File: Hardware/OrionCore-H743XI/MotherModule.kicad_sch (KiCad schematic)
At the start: 1 part, among them U2 STM32H743XIHx

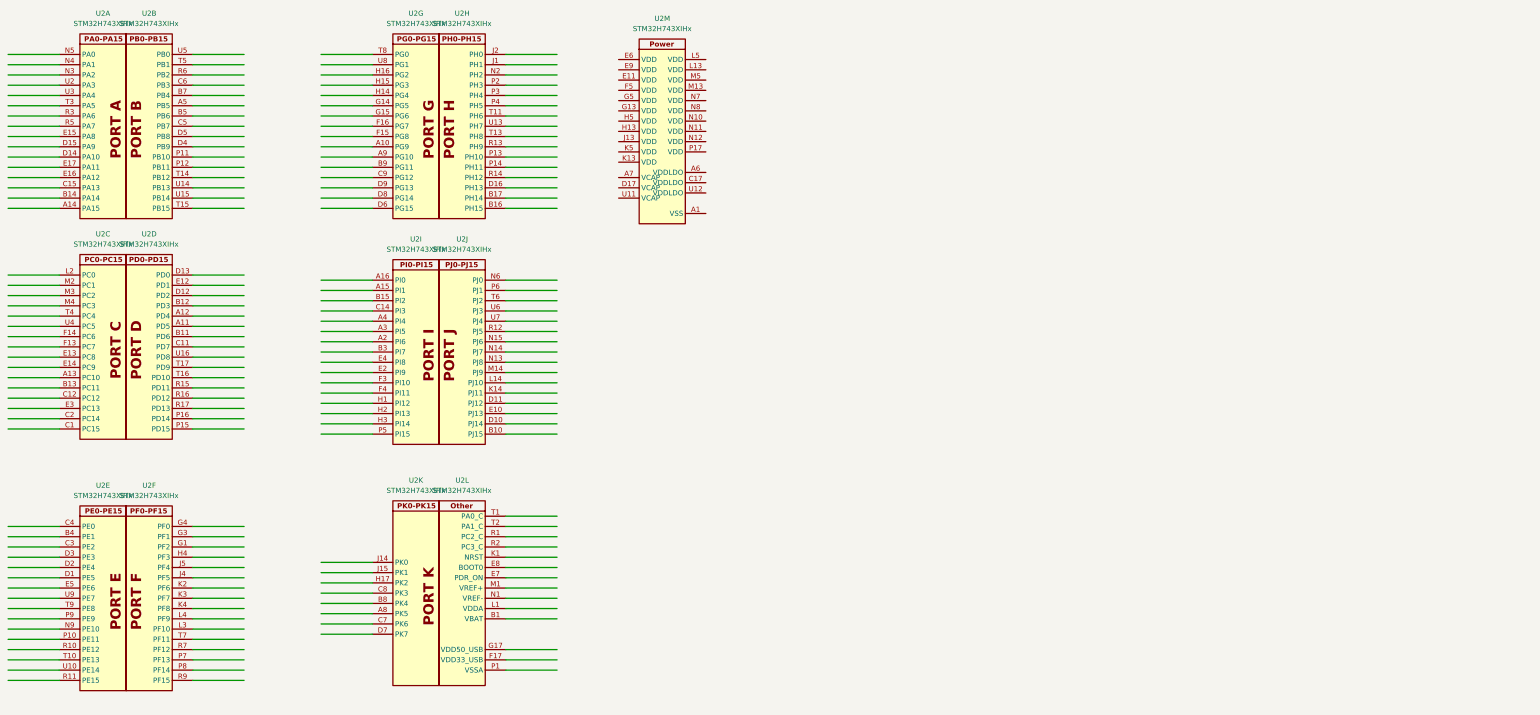
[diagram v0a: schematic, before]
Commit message: Update SDRAM, RGB LCD, QSPI Flash Pin
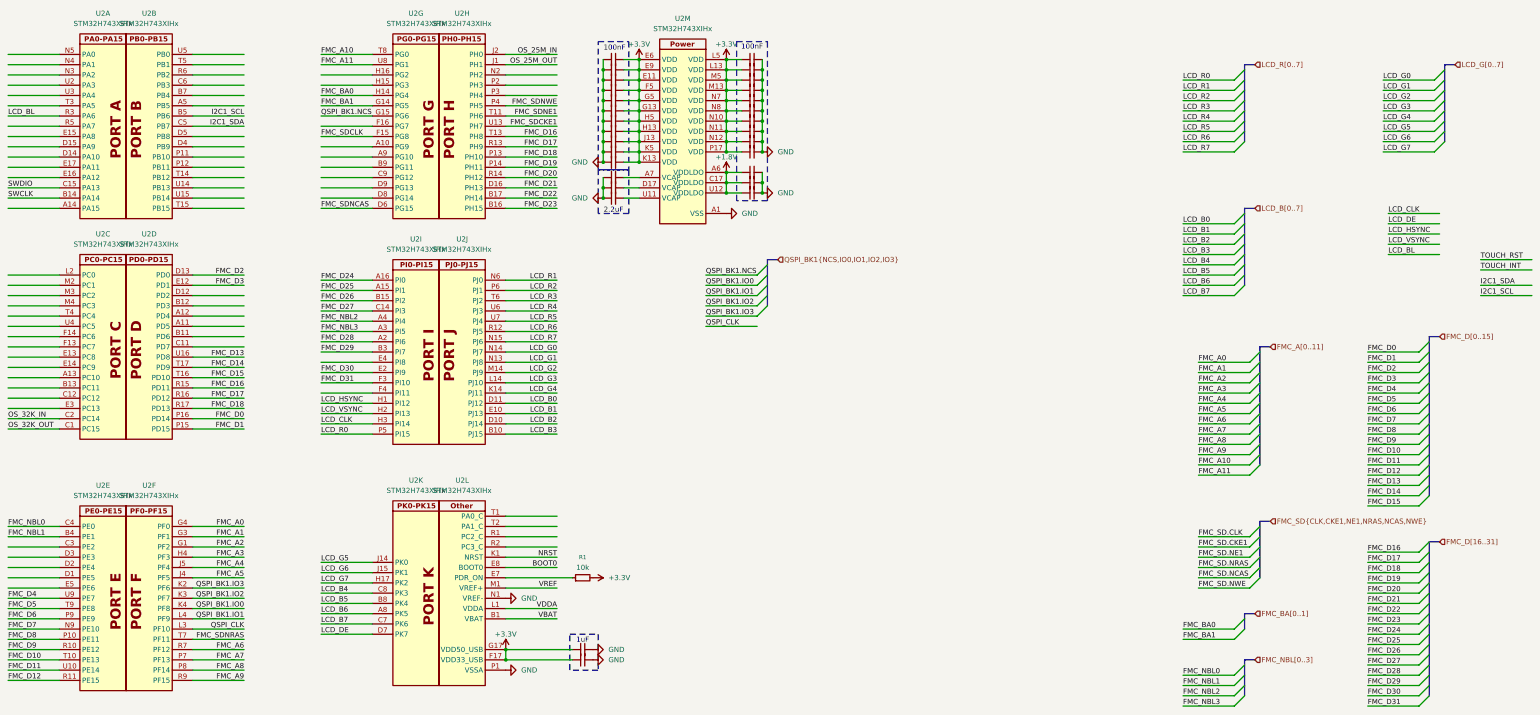
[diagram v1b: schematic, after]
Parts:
- added C1, C2: 1uF, Capacitor_SMD:C_0201_0603Metric, symbol Device:C_Small
- added C10, C11, C12, C13, C14, C15, C16, C17, C18, C19, C20, C21, C22, C23, C24, C25, C26, C3, C4, C5, C6, C7, C8, C9: 100nF, Capacitor_SMD:C_0201_0603Metric, symbol Device:C_Small
- added C27, C28, C29: 2.2uF, Capacitor_SMD:C_0402_1005Metric, symbol Device:C_Small
- added R1: 10k, Resistor_SMD:R_0201_0603Metric, symbol Device:R_Small
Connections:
- net VBAT: now reaches U2.B1 (VBAT)
- net at U2.E7 (PDR_ON): now also R1.1
- net BOOT0: now reaches U2.E8 (BOOT0)
- net +3.3V: now reaches U2.F17 (VDD33_USB)
- net +3.3V: now also U2.E11 (VDD), U2.E6 (VDD), U2.E9 (VDD), U2.F5 (VDD), U2.G13 (VDD), U2.G17 (VDD50_USB), U2.G5 (VDD), U2.H13 (VDD), U2.H5 (VDD), U2.J13 (VDD), U2.K13 (VDD), U2.K5 (VDD), U2.L13 (VDD), U2.L5 (VDD), U2.M13 (VDD), U2.M5 (VDD), U2.N10 (VDD), U2.N11 (VDD), U2.N12 (VDD), U2.N7 (VDD), U2.N8 (VDD), U2.P17 (VDD), C1.1, C10.1, C11.1, C12.1, C13.1, C14.1, C15.1, C16.1, C17.1, C18.1, C19.1, C2.1, C20.1, C21.1, C22.1, C23.1, C24.1, C25.1, C26.1, C6.1, C7.1, C8.1, C9.1, R1.2
- net NRST: now reaches U2.K1 (NRST)
- net VDDA: now reaches U2.L1 (VDDA)
- net VREF: now reaches U2.M1 (VREF+)
- net GND: now reaches U2.N1 (VREF-)
- net GND: now also U2.A1 (VSS), U2.A17 (VSS), U2.B2 (VSS), U2.B6 (VSS), U2.C10 (VSS), U2.C13 (VSS), U2.C16 (VSS), U2.F1 (VSS), U2.F2 (VSS), U2.G10 (VSS), U2.G11 (VSS), U2.G16 (VSS), U2.G2 (VSS), U2.G7 (VSS), U2.G8 (VSS), U2.G9 (VSS), U2.H10 (VSS), U2.H11 (VSS), U2.H7 (VSS), U2.H8 (VSS), U2.H9 (VSS), U2.J10 (VSS), U2.J11 (VSS), U2.J16 (VSS), U2.J17 (VSS), U2.J3 (VSS), U2.J7 (VSS), U2.J8 (VSS), U2.J9 (VSS), U2.K10 (VSS), U2.K11 (VSS), U2.K15 (VSS), U2.K7 (VSS), U2.K8 (VSS), U2.K9 (VSS), U2.L10 (VSS), U2.L11 (VSS), U2.L15 (VSS), U2.L7 (VSS), U2.L8 (VSS), U2.L9 (VSS), U2.M15 (VSS), U2.N16 (VSS), U2.P1 (VSSA), U2.R4 (VSS), U2.R8 (VSS), U2.T12 (VSS), U2.U1 (VSS), U2.U17 (VSS), C1.2, C10.2, C11.2, C12.2, C13.2, C14.2, C15.2, C16.2, C17.2, C18.2, C19.2, C2.2, C20.2, C21.2, C22.2, C23.2, C24.2, C25.2, C26.2, C27.1, C28.1, C29.1, C3.2, C4.2, C5.2, C6.2, C7.2, C8.2, C9.2
- net FMC_D25: now reaches U2.A15 (PI1)
- net FMC_D24: now reaches U2.A16 (PI0)
- net FMC_D28: now reaches U2.A2 (PI6)
- net FMC_NBL3: now reaches U2.A3 (PI5)
- net FMC_NBL2: now reaches U2.A4 (PI4)
- net FMC_D26: now reaches U2.B15 (PI2)
- net FMC_D29: now reaches U2.B3 (PI7)
- net FMC_D27: now reaches U2.C14 (PI3)
- net FMC_D30: now reaches U2.E2 (PI9)
- net FMC_D31: now reaches U2.F3 (PI10)
- net LCD_HSYNC: now reaches U2.H1 (PI12)
- net LCD_VSYNC: now reaches U2.H2 (PI13)
- net LCD_CLK: now reaches U2.H3 (PI14)
- net LCD_R0: now reaches U2.P5 (PI15)
- net FMC_NBL1: now reaches U2.B4 (PE1)
- net FMC_NBL0: now reaches U2.C4 (PE0)
- net FMC_D7: now reaches U2.N9 (PE10)
- net FMC_D8: now reaches U2.P10 (PE11)
- net FMC_D6: now reaches U2.P9 (PE9)
- net FMC_D9: now reaches U2.R10 (PE12)
- net FMC_D12: now reaches U2.R11 (PE15)
- net FMC_D10: now reaches U2.T10 (PE13)
- net FMC_D5: now reaches U2.T9 (PE8)
- net FMC_D11: now reaches U2.U10 (PE14)
- net FMC_D4: now reaches U2.U9 (PE7)
- net SWCLK: now reaches U2.B14 (PA14)
- net SWDIO: now reaches U2.C15 (PA13)
- net LCD_BL: now reaches U2.R3 (PA6)
- net FMC_D2: now reaches U2.D13 (PD0)
- net FMC_D3: now reaches U2.E12 (PD1)
- net FMC_D1: now reaches U2.P15 (PD15)
- net FMC_D0: now reaches U2.P16 (PD14)
- net FMC_D16: now reaches U2.R15 (PD11)
- net FMC_D16: now also U2.T13 (PH8)
- net FMC_D17: now reaches U2.R16 (PD12)
- net FMC_D17: now also U2.R13 (PH9)
- net FMC_D18: now reaches U2.R17 (PD13)
- net FMC_D18: now also U2.P13 (PH10)
- net FMC_D15: now reaches U2.T16 (PD10)
- net FMC_D14: now reaches U2.T17 (PD9)
- net FMC_D13: now reaches U2.U16 (PD8)
- net LCD_B6: now reaches U2.A8 (PK5)
- net LCD_B5: now reaches U2.B8 (PK4)
- net LCD_B7: now reaches U2.C7 (PK6)
- net LCD_B4: now reaches U2.C8 (PK3)
- net LCD_DE: now reaches U2.D7 (PK7)
- net LCD_G7: now reaches U2.H17 (PK2)
- net LCD_G5: now reaches U2.J14 (PK0)
- net LCD_G6: now reaches U2.J15 (PK1)
- net OS_32K_OUT: now reaches U2.C1 (PC15)
- net OS_32K_IN: now reaches U2.C2 (PC14)
- net I2C1_SCL: now reaches U2.B5 (PB6)
- net I2C1_SDA: now reaches U2.C5 (PB7)
- net FMC_D23: now reaches U2.B16 (PH15)
- net FMC_D22: now reaches U2.B17 (PH14)
- net FMC_D21: now reaches U2.D16 (PH13)
- net OS_25M_OUT: now reaches U2.J1 (PH1)
- net OS_25M_IN: now reaches U2.J2 (PH0)
- net FMC_D19: now reaches U2.P14 (PH11)
- net FMC_SDNWE: now reaches U2.P4 (PH5)
- net FMC_D20: now reaches U2.R14 (PH12)
- net FMC_SDNE1: now reaches U2.T11 (PH6)
- net FMC_SDCKE1: now reaches U2.U13 (PH7)
- net +1.8V: now reaches U2.A6 (VDDLDO)
- net +1.8V: now also U2.C17 (VDDLDO), U2.U12 (VDDLDO), C3.1, C4.1, C5.1
- net at U2.A7 (VCAP): now also C29.2
- net at U2.D17 (VCAP): now also C28.2
- net at U2.U11 (VCAP): now also C27.2
- net FMC_SDNCAS: now reaches U2.D6 (PG15)
- net FMC_SDCLK: now reaches U2.F15 (PG8)
- net FMC_BA1: now reaches U2.G14 (PG5)
- net QSPI_BK1.NCS: now reaches U2.G15 (PG6)
- net FMC_BA0: now reaches U2.H14 (PG4)
- net FMC_A10: now reaches U2.T8 (PG0)
- net FMC_A11: now reaches U2.U8 (PG1)
- net LCD_B3: now reaches U2.B10 (PJ15)
- net LCD_B2: now reaches U2.D10 (PJ14)
- net LCD_B0: now reaches U2.D11 (PJ12)
- net LCD_B1: now reaches U2.E10 (PJ13)
- net LCD_G4: now reaches U2.K14 (PJ11)
- net LCD_G3: now reaches U2.L14 (PJ10)
- net LCD_G2: now reaches U2.M14 (PJ9)
- net LCD_G1: now reaches U2.N13 (PJ8)
- net LCD_G0: now reaches U2.N14 (PJ7)
- net LCD_R7: now reaches U2.N15 (PJ6)
- net LCD_R1: now reaches U2.N6 (PJ0)
- net LCD_R2: now reaches U2.P6 (PJ1)
- net LCD_R6: now reaches U2.R12 (PJ5)
- net LCD_R3: now reaches U2.T6 (PJ2)
- net LCD_R4: now reaches U2.U6 (PJ3)
- net LCD_R5: now reaches U2.U7 (PJ4)
- net FMC_A2: now reaches U2.G1 (PF2)
- net FMC_A1: now reaches U2.G3 (PF1)
- net FMC_A0: now reaches U2.G4 (PF0)
- net FMC_A3: now reaches U2.H4 (PF3)
- net FMC_A5: now reaches U2.J4 (PF5)
- net FMC_A4: now reaches U2.J5 (PF4)
- net QSPI_BK1.IO3: now reaches U2.K2 (PF6)
- net QSPI_BK1.IO2: now reaches U2.K3 (PF7)
- net QSPI_BK1.IO0: now reaches U2.K4 (PF8)
- net QSPI_CLK: now reaches U2.L3 (PF10)
- net QSPI_BK1.IO1: now reaches U2.L4 (PF9)
- net FMC_A7: now reaches U2.P7 (PF13)
- net FMC_A8: now reaches U2.P8 (PF14)
- net FMC_A6: now reaches U2.R7 (PF12)
- net FMC_A9: now reaches U2.R9 (PF15)
- net FMC_SDNRAS: now reaches U2.T7 (PF11)
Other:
- note added: "100nF"
- note added: "1uF"
- note added: "2.2uF"
- moved on the sheet: U2M

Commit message: feat: update dual qspi
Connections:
- net QSPI_BK2.NCS: now reaches U2.B13 (PC11)
- net QSPI_BK2.IO0: now reaches U2.N2 (PH2)
- net QSPI_BK2.IO1: now reaches U2.P2 (PH3)
- net QSPI_BK2.IO2: now reaches U2.A10 (PG9)
- net QSPI_BK2.IO3: now reaches U2.D8 (PG14)
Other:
- company: (none) -> Peakors
- title: (none) -> OrionCore
